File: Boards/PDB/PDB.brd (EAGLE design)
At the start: 160 x 101.6 mm, 59 parts, among them Q1 NMOS, Q2 IRFML8244, Q3 PMOS, Q4 PMOS, Q5 PMOS

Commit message: I don't know
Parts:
- removed FUSE1, FUSE10, FUSE2, FUSE3, FUSE4, FUSE5, FUSE6, FUSE7, FUSE8, FUSE9: FUSE_HOLDER_SMD, pie:FUSE_HOLDER_SMD
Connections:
- removed net VOUT1: CONN1.PIN2, FUSE1.P$1_DOWN, FUSE1.P$1_UP
- removed net VOUT10: CONN10.P$1, FUSE10.P$1_DOWN, FUSE10.P$1_UP
- removed net VOUT2: CONN2.PIN2, FUSE2.P$1_DOWN, FUSE2.P$1_UP
- removed net VOUT3: CONN3.PIN2, FUSE3.P$1_DOWN, FUSE3.P$1_UP
- removed net VOUT4: CONN4.PIN2, FUSE4.P$2_DOWN, FUSE4.P$2_UP
- removed net VOUT5: CONN5.PIN2, FUSE5.P$2_DOWN, FUSE5.P$2_UP
- removed net VOUT6: CONN6.PIN2, FUSE6.P$2_DOWN, FUSE6.P$2_UP
- removed net VOUT7: CONN7.P$1, FUSE7.P$2_DOWN, FUSE7.P$2_UP
- removed net VOUT8: CONN9.P$1, FUSE8.P$1_DOWN, FUSE8.P$1_UP
- removed net VOUT9: CONN8.P$1, FUSE9.P$2_DOWN, FUSE9.P$2_UP
- net 12V: now also CONN1.PIN2, CONN2.PIN2, CONN3.PIN2, CONN4.PIN2, CONN5.PIN2, CONN6.PIN2; no longer FUSE1.P$2_DOWN, FUSE1.P$2_UP, FUSE2.P$2_DOWN, FUSE2.P$2_UP, FUSE3.P$2_DOWN, FUSE3.P$2_UP, FUSE4.P$1_DOWN, FUSE4.P$1_UP, FUSE5.P$1_DOWN, FUSE5.P$1_UP, FUSE6.P$1_DOWN, FUSE6.P$1_UP
- net 5V: now also CONN10.P$1, CONN7.P$1, CONN8.P$1, CONN9.P$1; no longer FUSE10.P$2_DOWN, FUSE10.P$2_UP, FUSE7.P$1_DOWN, FUSE7.P$1_UP, FUSE8.P$2_DOWN, FUSE8.P$2_UP, FUSE9.P$1_DOWN, FUSE9.P$1_UP
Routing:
- net 5V: track 177.3 -> 176.8 mm
- removed copper zone on layer 1, net VOUT1
- removed copper zone on layer 1, net VOUT10
- removed copper zone on layer 1, net VOUT2
- removed copper zone on layer 1, net VOUT3
- removed copper zone on layer 1, net VOUT4
- removed copper zone on layer 1, net VOUT5
- removed copper zone on layer 1, net VOUT6
- removed copper zone on layer 1, net VOUT7
- removed copper zone on layer 1, net VOUT8
- removed copper zone on layer 1, net VOUT9

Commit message: REV B PLEASE WORK
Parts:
- removed U$7: BUCK_CONVERTER_5V, pie:BUCK_CONVERTER_5V
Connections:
- net 12V: no longer U$7.IN+
- net 5V: no longer U$7.OUT+
- net GND: no longer U$7.IN-, U$7.OUT-
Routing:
- net GND: track 52.3 -> 48.5 mm, vias 8 -> 10
- net 5V: vias 1 -> 2
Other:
- board text added: "5V OUT -"
- board text added: "5V OUT+"
- board text added: "IN -"
- board text added: "IN+"
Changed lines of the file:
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@@
 <text x="80.264" y="90.932" size="1.778" layer="21">-</text>
 <text x="60.706" y="90.932" size="1.778" layer="21">-</text>
+<text x="128.016" y="73.914" size="1.778" layer="21">IN+</text>
+<text x="128.27" y="68.326" size="1.778" layer="21" font="vector">IN -</text>
+<text x="128.27" y="63.246" size="1.778" layer="21">5V OUT -</text>
+<text x="128.27" y="57.658" size="1.778" layer="21">5V OUT+</text>
 </plain>
 <attributes>
@@
 <element name="U$5" library="pie" package="STAND-OFF" value="" x="20.32" y="61.722"/>
 <element name="U$6" library="pie" package="PIE-LOGO-SMALL" value="" x="39.878" y="81.28"/>
-<element name="U$7" library="pie" package="BUCK_CONVERTER_5V" value="BUCK_CONVERTER_5V" x="155.702" y="66.294" smashed="yes" rot="R90"/>
 <element name="JP1" library="pie" package="XH_CONNECTOR_4POS_2.5MM" value="XH_CONN" x="19.812" y="93.218" smashed="yes" rot="R270">
 <attribute name="PIE-INT-REF-NUM" value="XH-4POS" x="71.882" y="104.648" size="1.778" layer="27" rot="R270" display="off"/>
@@
 <polygon width="1.1938" layer="16" rank="6">
 <vertex x="0" y="101.6"/>
-<vertex x="160.02" y="101.6"/>
+<vertex x="159.766" y="101.6"/>
 <vertex x="160.02" y="0"/>
 <vertex x="0" y="0"/>
@@
 <contactref element="CONN5" pad="PIN1"/>
 <contactref element="CONN6" pad="PIN1"/>
-<contactref element="U$7" pad="IN-"/>
-<contactref element="U$7" pad="OUT-"/>
 <contactref element="R5" pad="1"/>
 <contactref element="R6" pad="1"/>
@@
 <wire x1="10.922" y1="22.098" x2="10.58" y2="22.098" width="0.4064" layer="1"/>
 <wire x1="10.58" y1="22.098" x2="9.906" y2="21.424" width="0.4064" layer="1"/>
-<wire x1="123.952" y1="63.754" x2="123.952" y2="67.564" width="1.27" layer="16"/>
 <contactref element="CONN7" pad="P$2"/>
 <contactref element="CONN8" pad="P$2"/>
 <contactref element="CONN9" pad="P$2"/>
 <contactref element="CONN10" pad="P$2"/>
+<via x="123.952" y="69.088" extent="1-16" drill="2.8" diameter="3.81"/>
+<via x="123.952" y="64.008" extent="1-16" drill="2.8" diameter="3.81"/>
 </signal>
 <signal name="12V">
@@
 </polygon>
 <contactref element="CIRCUIT_BREAKER" pad="P$2"/>
-<contactref element="U$7" pad="IN+"/>
 <contactref element="CONN1" pad="PIN2"/>
 <polygon width="1.1938" layer="1" isolate="1.27">
@@
 <vertex x="142.24" y="16.51"/>
 </polygon>
+<via x="123.952" y="74.168" extent="1-16" drill="2.8" diameter="3.81"/>
 </signal>
 <signal name="BAT">
@@
 </signal>
 <signal name="5V">
-<contactref element="U$7" pad="OUT+"/>
 <polygon width="1.1938" layer="1">
 <vertex x="52.07" y="87.376"/>
@@
 </polygon>
 <contactref element="CONN10" pad="P$1"/>
+<via x="123.952" y="58.674" extent="1-16" drill="2.8" diameter="3.81"/>
 </signal>
 <signal name="IO1">

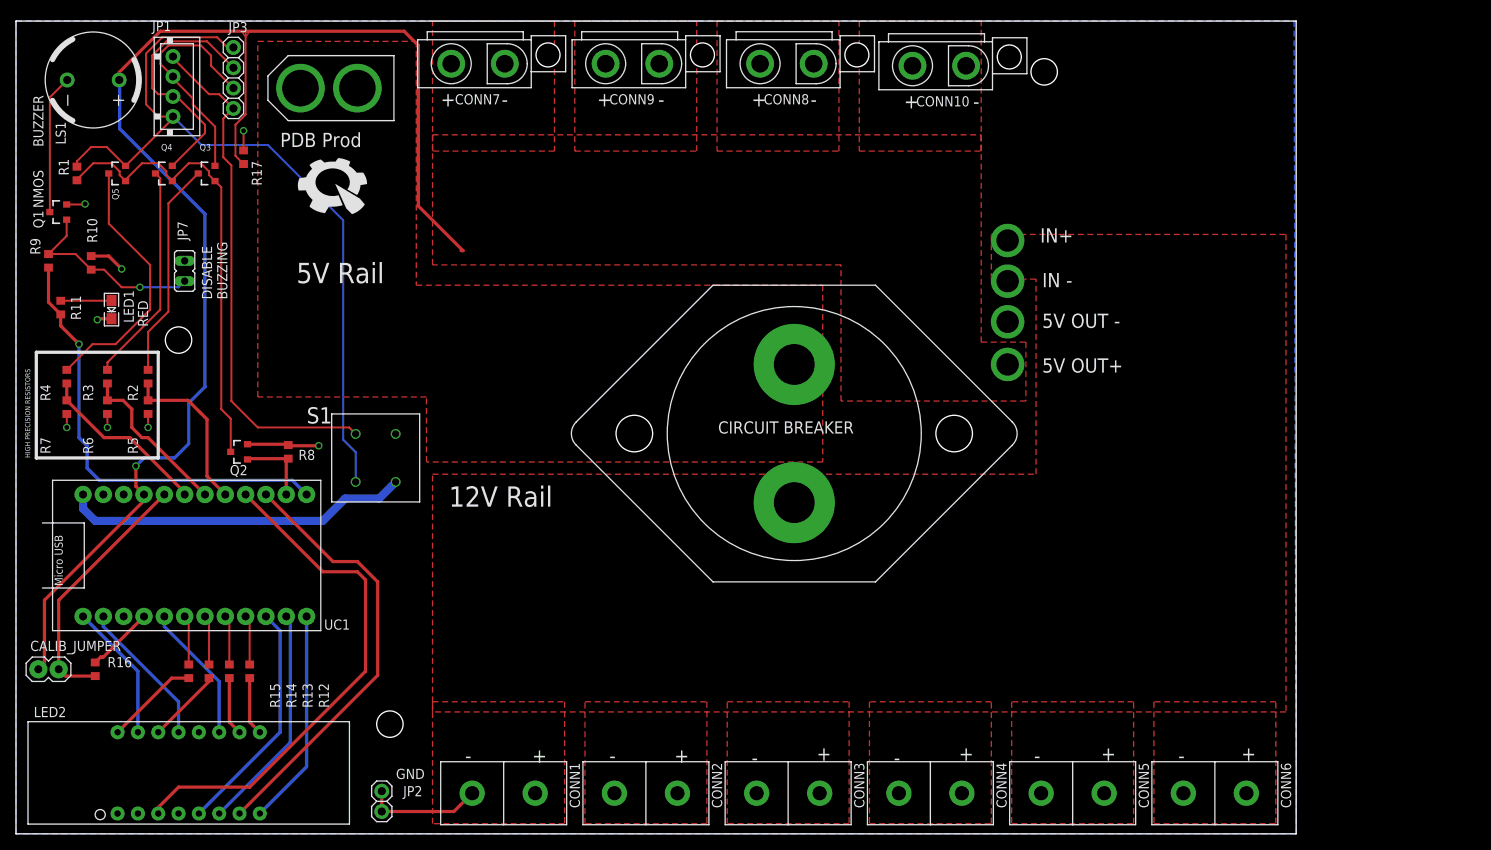
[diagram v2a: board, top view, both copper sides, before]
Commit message: Added back 5V buck and added caps. DRC clean
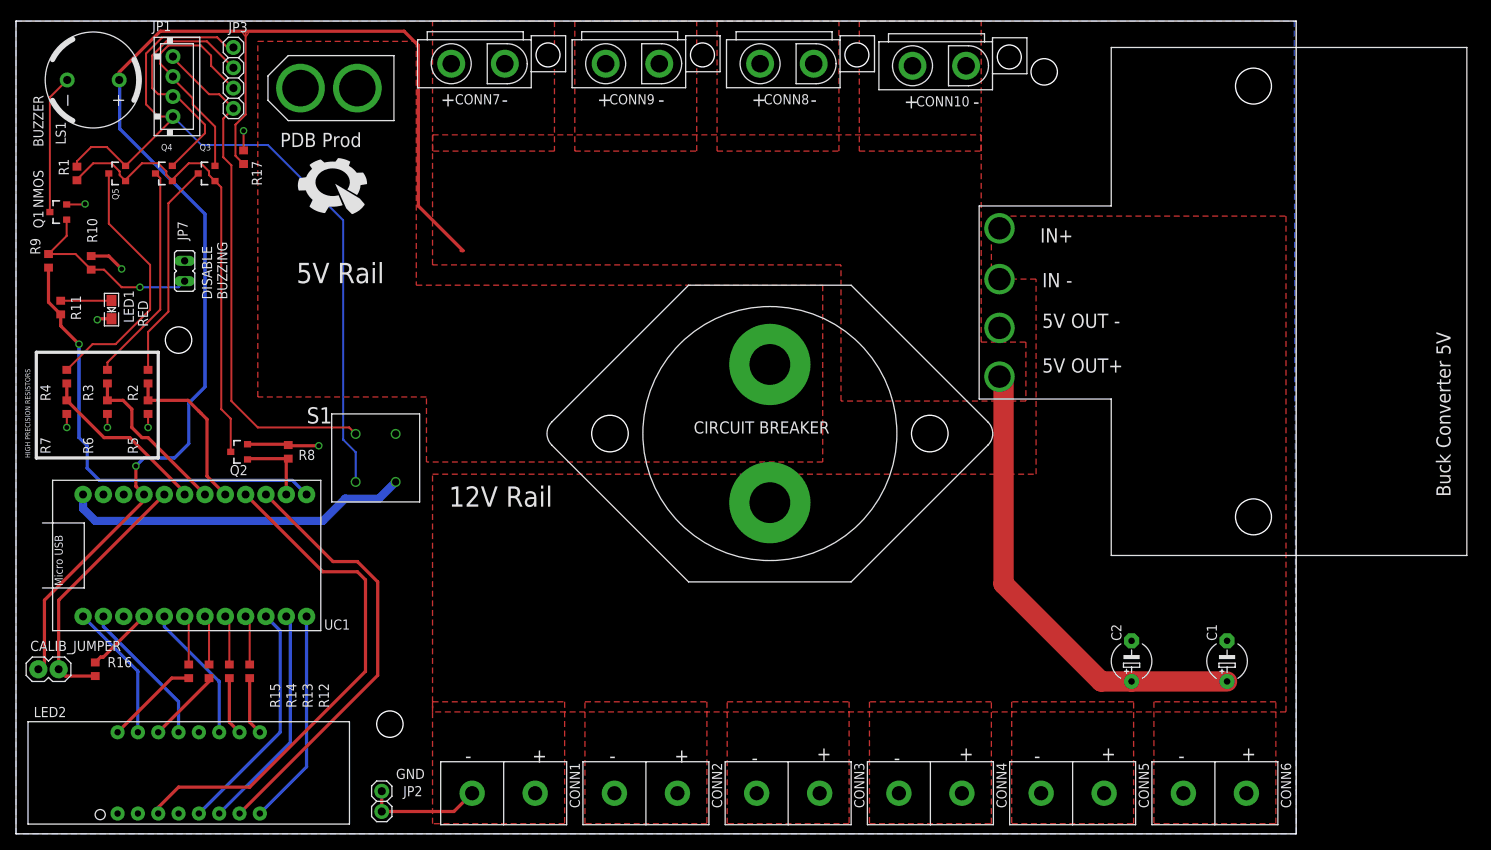
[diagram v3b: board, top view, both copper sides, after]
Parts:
- added C1: 1uF, rcl:E5-5
- added C2: 10uF, rcl:E5-5
- added U$1: BUCK_CONVERTER_5V, pie:BUCK_CONVERTER_5V
- moved CIRCUIT_BREAKER 3.05 mm to (94.2, 50.0)
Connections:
- net 12V: now also U$1.IN+
- net 5V: now also C1.+, C2.+, U$1.OUT+
- net GND: now also C1.-, C2.-, U$1.IN-, U$1.OUT-
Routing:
- net 5V: track 176.8 -> 235.9 mm, vias 2 -> 1
- net GND: vias 10 -> 8

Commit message: Please, PDB, please work. Also I updated ATX connector.
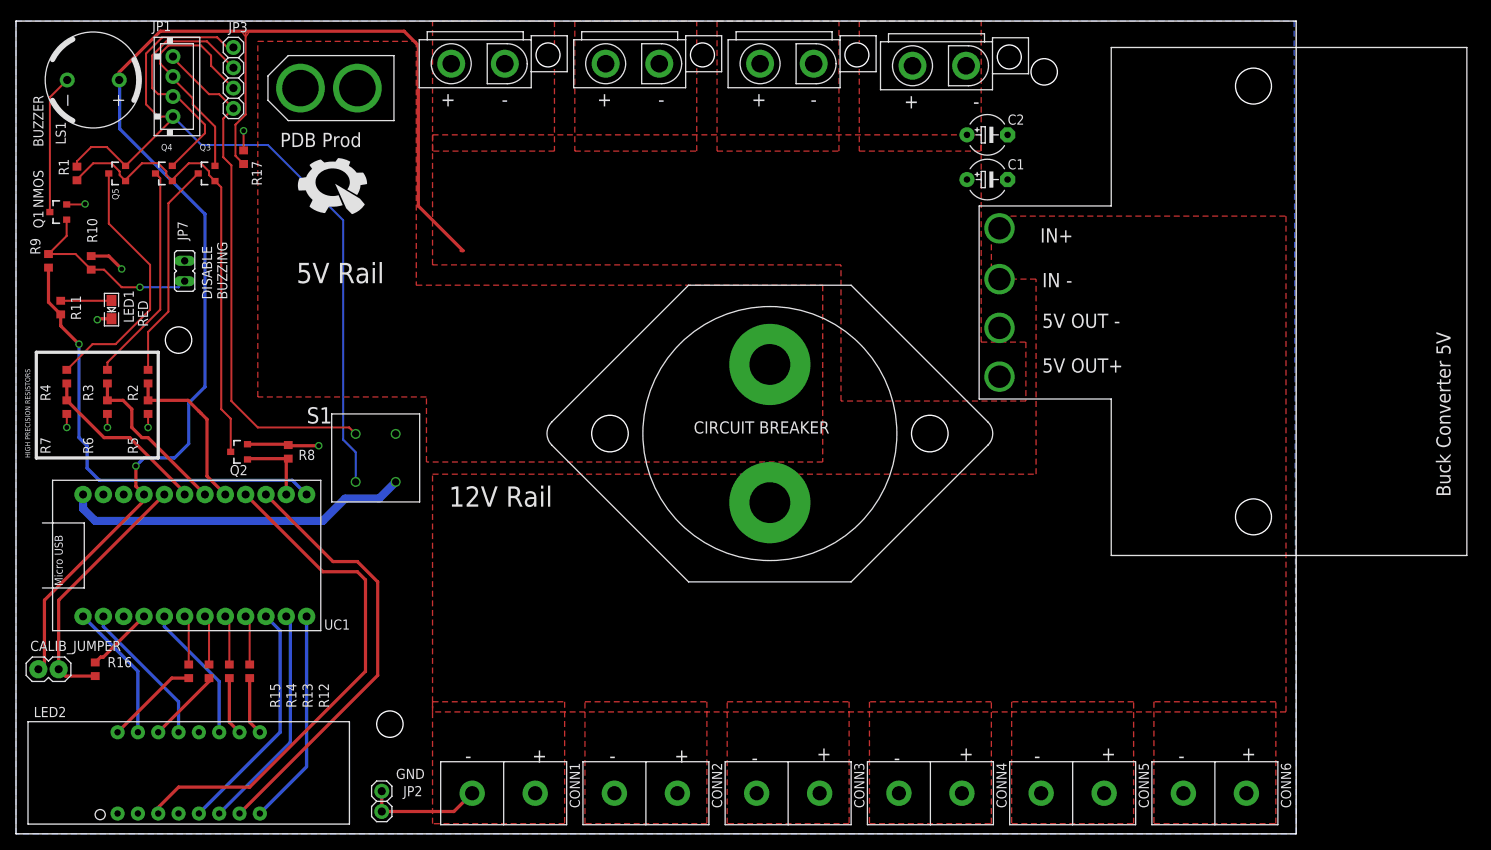
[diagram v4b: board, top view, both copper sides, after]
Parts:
- R1, R16, R2, R5, R6, R7, R8: value 10k -> >VALUE
- R10: value 100k -> >VALUE
- R11: value 130 -> >VALUE
- R12, R13, R14, R15: value 330 -> >VALUE
- R17: value 3k -> >VALUE
- R3: value 30k -> >VALUE
- R4: value 51k -> >VALUE
- R9: value 1k -> >VALUE
- moved C2 68.2 mm to (121.4, 87.4), turned to 0 degrees
- moved C1 67.2 mm to (121.4, 81.8), turned to 0 degrees
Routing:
- net 5V: track 235.9 -> 176.8 mm

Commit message: I hate my life
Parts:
- R1, R16, R2, R5, R6, R7, R8: value >VALUE -> 10k
- R10: value >VALUE -> 100k
- R11: value >VALUE -> 130
- R12, R13, R14, R15: value >VALUE -> 330
- R17: value >VALUE -> 3k
- R3: value >VALUE -> 30k
- R4: value >VALUE -> 51k
- R9: value >VALUE -> 1k
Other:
- board text added: "Copyright (c) 2016, Pioneers in Engineering All rights reserved. Design by: Tobin H., Doug H, Nick W, Adilet P This design is open source hardware. For more information, visit github.com/pioneers/SmartSensors"
- board text removed: "Copyright (c) 2016, Pioneers in Engineering All rights reserved. Design by: Sharabesh R, Mohammed H, Tobin H., Doug H This design is open source hardware. For more information, visit github.com/pioneers/SmartSensors"

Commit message: finished rev1 pdb:
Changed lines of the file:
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@@
 <?xml version="1.0" encoding="utf-8"?>
 <!DOCTYPE eagle SYSTEM "eagle.dtd">
-<eagle version="8.3.2">
+<eagle version="9.3.0">
 <drawing>
 <settings>
@@
 <param name="dpMaxLengthDifference" value="0.5mm"/>
 <param name="dpGapFactor" value="2.5"/>
-<param name="checkGrid" value="0"/>
 <param name="checkAngle" value="1"/>
 <param name="checkFont" value="1"/>
 <param name="checkRestrict" value="1"/>
+<param name="checkStop" value="0"/>
+<param name="checkValues" value="0"/>
+<param name="checkNames" value="1"/>
+<param name="checkWireStubs" value="1"/>
+<param name="checkPolygonWidth" value="0"/>
 <param name="useDiameter" value="15"/>
 <param name="maxErrors" value="50"/>
@@
 </autorouter>
 <elements>
-<element name="CONN3" library="pie" package="ANDERSON_VERTICAL" value="ANDERSONVERTICAL" x="96.52" y="5.08" rot="R270">
+<element name="CONN3" library="pie" package="ANDERSON_VERTICAL" value="ANDERSONVERTICAL" x="96.52" y="5.08" smashed="yes" rot="R270">
+<attribute name="NAME" x="104.775" y="8.89" size="1.27" layer="25" font="vector" ratio="10" rot="R270"/>
 <attribute name="PIE-INT-REF-NUM" value="Anderson" x="96.52" y="5.08" size="1.778" layer="27" rot="R270" display="off"/>
 </element>
-<element name="CONN1" library="pie" package="ANDERSON_VERTICAL" value="ANDERSONVERTICAL" x="60.96" y="5.08" rot="R270">
+<element name="CONN1" library="pie" package="ANDERSON_VERTICAL" value="ANDERSONVERTICAL" x="60.96" y="5.08" smashed="yes" rot="R270">
+<attribute name="NAME" x="69.215" y="8.89" size="1.27" layer="25" font="vector" ratio="10" rot="R270"/>
 <attribute name="PIE-INT-REF-NUM" value="Anderson" x="60.96" y="5.08" size="1.778" layer="27" rot="R270" display="off"/>
 </element>
-<element name="CONN2" library="pie" package="ANDERSON_VERTICAL" value="ANDERSONVERTICAL" x="78.74" y="5.08" rot="R270">
+<element name="CONN2" library="pie" package="ANDERSON_VERTICAL" value="ANDERSONVERTICAL" x="78.74" y="5.08" smashed="yes" rot="R270">
+<attribute name="NAME" x="86.995" y="8.89" size="1.27" layer="25" font="vector" ratio="10" rot="R270"/>
 <attribute name="PIE-INT-REF-NUM" value="Anderson" x="78.74" y="5.08" size="1.778" layer="27" rot="R270" display="off"/>
 </element>
-<element name="CONN4" library="pie" package="ANDERSON_VERTICAL" value="ANDERSONVERTICAL" x="114.3" y="5.08" rot="R270">
+<element name="CONN4" library="pie" package="ANDERSON_VERTICAL" value="ANDERSONVERTICAL" x="114.3" y="5.08" smashed="yes" rot="R270">
+<attribute name="NAME" x="122.555" y="8.89" size="1.27" layer="25" font="vector" ratio="10" rot="R270"/>
 <attribute name="PIE-INT-REF-NUM" value="Anderson" x="114.3" y="5.08" size="1.778" layer="27" rot="R270" display="off"/>
 </element>
-<element name="XT60" library="pie" package="XT60CONNECTOR" value="XT60CONNECTOR" x="39.116" y="93.218" rot="R180">
+<element name="XT60" library="pie" package="XT60CONNECTOR" value="XT60CONNECTOR" x="39.116" y="93.218" smashed="yes" rot="R180">
 <attribute name="PARTNUMBER" value="PRT-10474 " x="39.116" y="93.218" size="1.778" layer="27" rot="R180" display="off"/>
 </element>
-<element name="CIRCUIT_BREAKER" library="pie" package="CIRC_BREAKER" value="CIRC_BREAKER" x="94.234" y="50.038">
+<element name="CIRCUIT_BREAKER" library="pie" package="CIRC_BREAKER" value="CIRC_BREAKER" x="94.234" y="50.038" smashed="yes">
 <attribute name="MANUF" value="WAYTEK" x="94.234" y="50.038" size="1.778" layer="27" display="off"/>
 <attribute name="MANUF-PN" value="46977" x="94.234" y="50.038" size="1.778" layer="27" display="off"/>
 </element>
-<element name="CONN5" library="pie" package="ANDERSON_VERTICAL" value="ANDERSONVERTICAL" x="132.08" y="5.08" rot="R270">
+<element name="CONN5" library="pie" package="ANDERSON_VERTICAL" value="ANDERSONVERTICAL" x="132.08" y="5.08" smashed="yes" rot="R270">
+<attribute name="NAME" x="140.335" y="8.89" size="1.27" layer="25" font="vector" ratio="10" rot="R270"/>
 <attribute name="PIE-INT-REF-NUM" value="Anderson" x="132.08" y="5.08" size="1.778" layer="27" rot="R270" display="off"/>
 </element>
-<element name="CONN6" library="pie" package="ANDERSON_VERTICAL" value="ANDERSONVERTICAL" x="149.86" y="5.08" rot="R270">
+<element name="CONN6" library="pie" package="ANDERSON_VERTICAL" value="ANDERSONVERTICAL" x="149.86" y="5.08" smashed="yes" rot="R270">
+<attribute name="NAME" x="158.115" y="8.89" size="1.27" layer="25" font="vector" ratio="10" rot="R270"/>
 <attribute name="PIE-INT-REF-NUM" value="Anderson" x="149.86" y="5.08" size="1.778" layer="27" rot="R270" display="off"/>
 </element>
-<element name="U$2" library="pie" package="STAND-OFF" value="" x="46.736" y="13.716"/>
-<element name="U$4" library="pie" package="STAND-OFF" value="" x="128.524" y="95.25" rot="R90"/>
-<element name="U$5" library="pie" package="STAND-OFF" value="" x="20.32" y="61.722"/>
-<element name="U$6" library="pie" package="PIE-LOGO-SMALL" value="" x="39.878" y="81.28"/>
+<element name="U$2" library="pie" package="STAND-OFF" value="" x="46.736" y="13.716" smashed="yes"/>
+<element name="U$4" library="pie" package="STAND-OFF" value="" x="128.524" y="95.25" smashed="yes" rot="R90"/>
+<element name="U$5" library="pie" package="STAND-OFF" value="" x="20.32" y="61.722" smashed="yes"/>
+<element name="U$6" library="pie" package="PIE-LOGO-SMALL" value="" x="39.878" y="81.28" smashed="yes"/>
 <element name="JP1" library="pie" package="XH_CONNECTOR_4POS_2.5MM" value="XH_CONN" x="19.812" y="93.218" smashed="yes" rot="R270">
 <attribute name="NAME" x="17.018" y="100.33" size="1.27" layer="25" font="vector" ratio="10"/>
@@
 <attribute name="VALUE" x="30.353" y="89.408" size="1.27" layer="27" font="vector" rot="R90"/>
 </element>
-<element name="CONN7" library="pie" package="ATX" value="ATX" x="57.404" y="96.266"/>
-<element name="CONN8" library="pie" package="ATX" value="ATX" x="96.012" y="96.266"/>
-<element name="CONN9" library="pie" package="ATX" value="ATX" x="76.708" y="96.266"/>
-<element name="CONN10" library="pie" package="ATX" value="ATX" x="115.062" y="96.012"/>
+<element name="CONN7" library="pie" package="ATX" value="ATX" x="57.404" y="96.266" smashed="yes"/>
+<element name="CONN8" library="pie" package="ATX" value="ATX" x="96.012" y="96.266" smashed="yes"/>
+<element name="CONN9" library="pie" package="ATX" value="ATX" x="76.708" y="96.266" smashed="yes"/>
+<element name="CONN10" library="pie" package="ATX" value="ATX" x="115.062" y="96.012" smashed="yes"/>
 <element name="C1" library="rcl" library_urn="urn:adsk.eagle:library:334" package="E5-5" package3d_urn="urn:adsk.eagle:package:23367/1" value="1uF" x="121.412" y="81.788" smashed="yes">
 <attribute name="NAME" x="123.952" y="83.058" size="1.27" layer="25" ratio="10"/>
 <attribute name="VALUE" x="123.952" y="79.248" size="1.27" layer="27" ratio="10"/>
 </element>
-<element name="C2" library="rcl" library_urn="urn:adsk.eagle:library:334" package="E5-5" package3d_urn="urn:adsk.eagle:package:23367/1" value="10uF" x="121.412" y="87.376"/>
-<element name="U$1" library="pie" package="BUCK_CONVERTER_5V" value="BUCK_CONVERTER_5V" x="154.686" y="66.548" rot="R90"/>
+<element name="C2" library="rcl" library_urn="urn:adsk.eagle:library:334" package="E5-5" package3d_urn="urn:adsk.eagle:package:23367/1" value="10uF" x="121.412" y="87.376" smashed="yes">
+<attribute name="NAME" x="123.952" y="88.646" size="1.27" layer="25" ratio="10"/>
+<attribute name="VALUE" x="123.952" y="84.836" size="1.27" layer="27" ratio="10"/>
+</element>
+<element name="U$1" library="pie" package="BUCK_CONVERTER_5V" value="BUCK_CONVERTER_5V" x="154.686" y="66.548" smashed="yes" rot="R90"/>
 </elements>
 <signals>
@@
 </signal>
 </signals>
+<mfgpreviewcolors>
+<mfgpreviewcolor name="soldermaskcolor" color="0xC8008000"/>
+<mfgpreviewcolor name="silkscreencolor" color="0xFFFEFEFE"/>
+<mfgpreviewcolor name="backgroundcolor" color="0xFF282828"/>
+<mfgpreviewcolor name="coppercolor" color="0xFFFFBF00"/>
+<mfgpreviewcolor name="substratecolor" color="0xFF786E46"/>
+</mfgpreviewcolors>
 <errors>
 </errors>
